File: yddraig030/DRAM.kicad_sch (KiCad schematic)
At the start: 6 parts, among them U1001 XC95108PQ100, U1002 74LS157

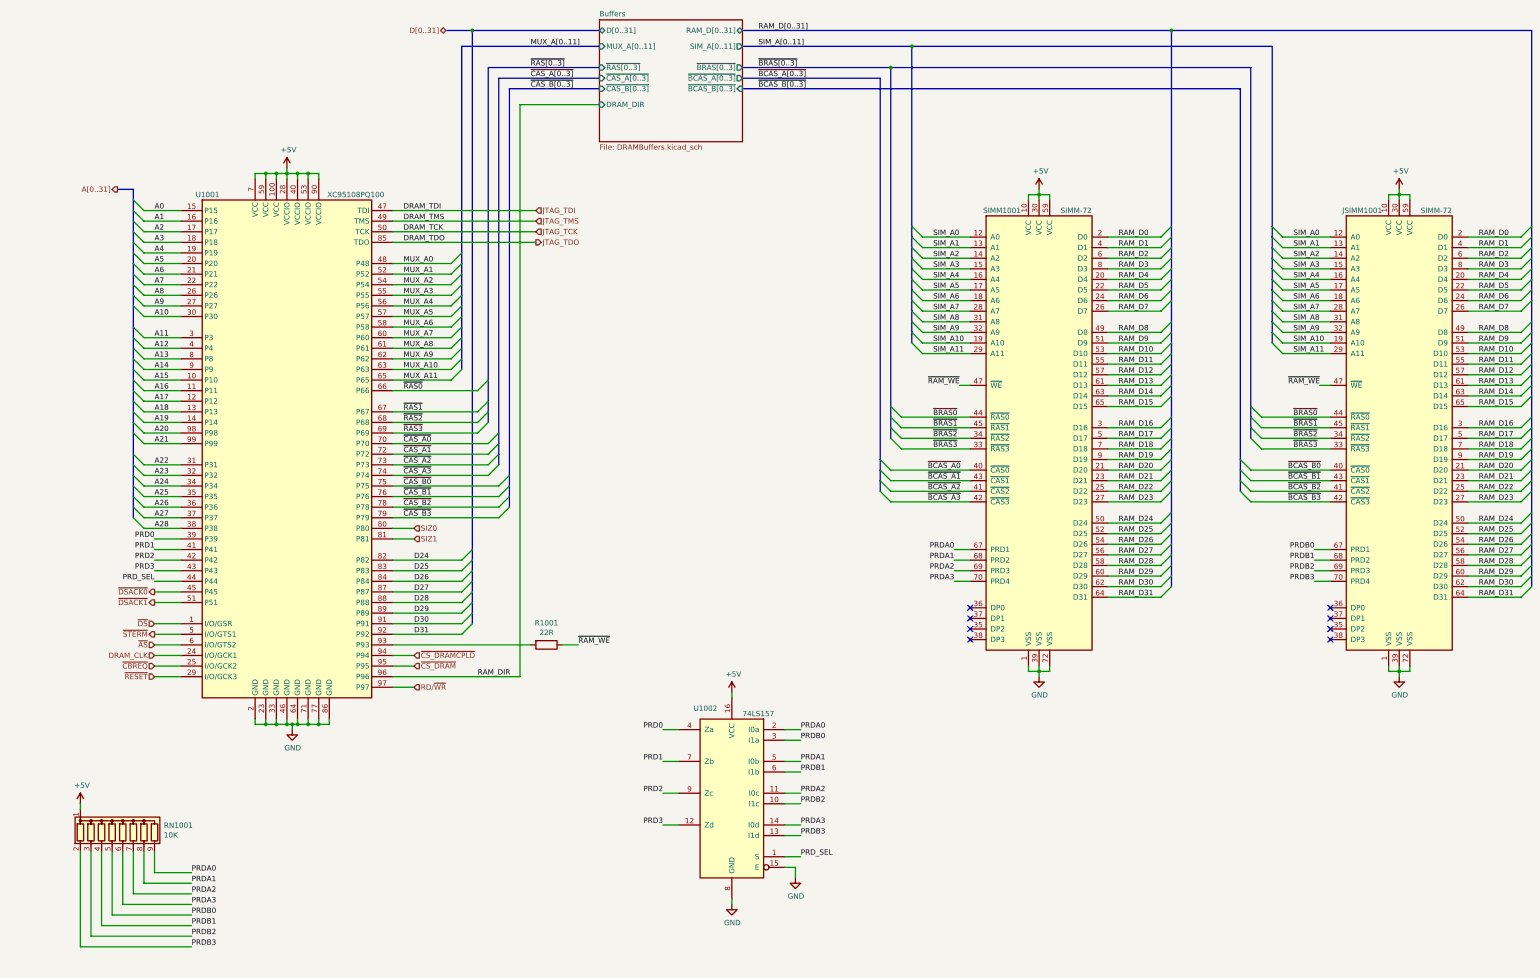
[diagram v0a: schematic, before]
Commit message: More changes to the 030 board
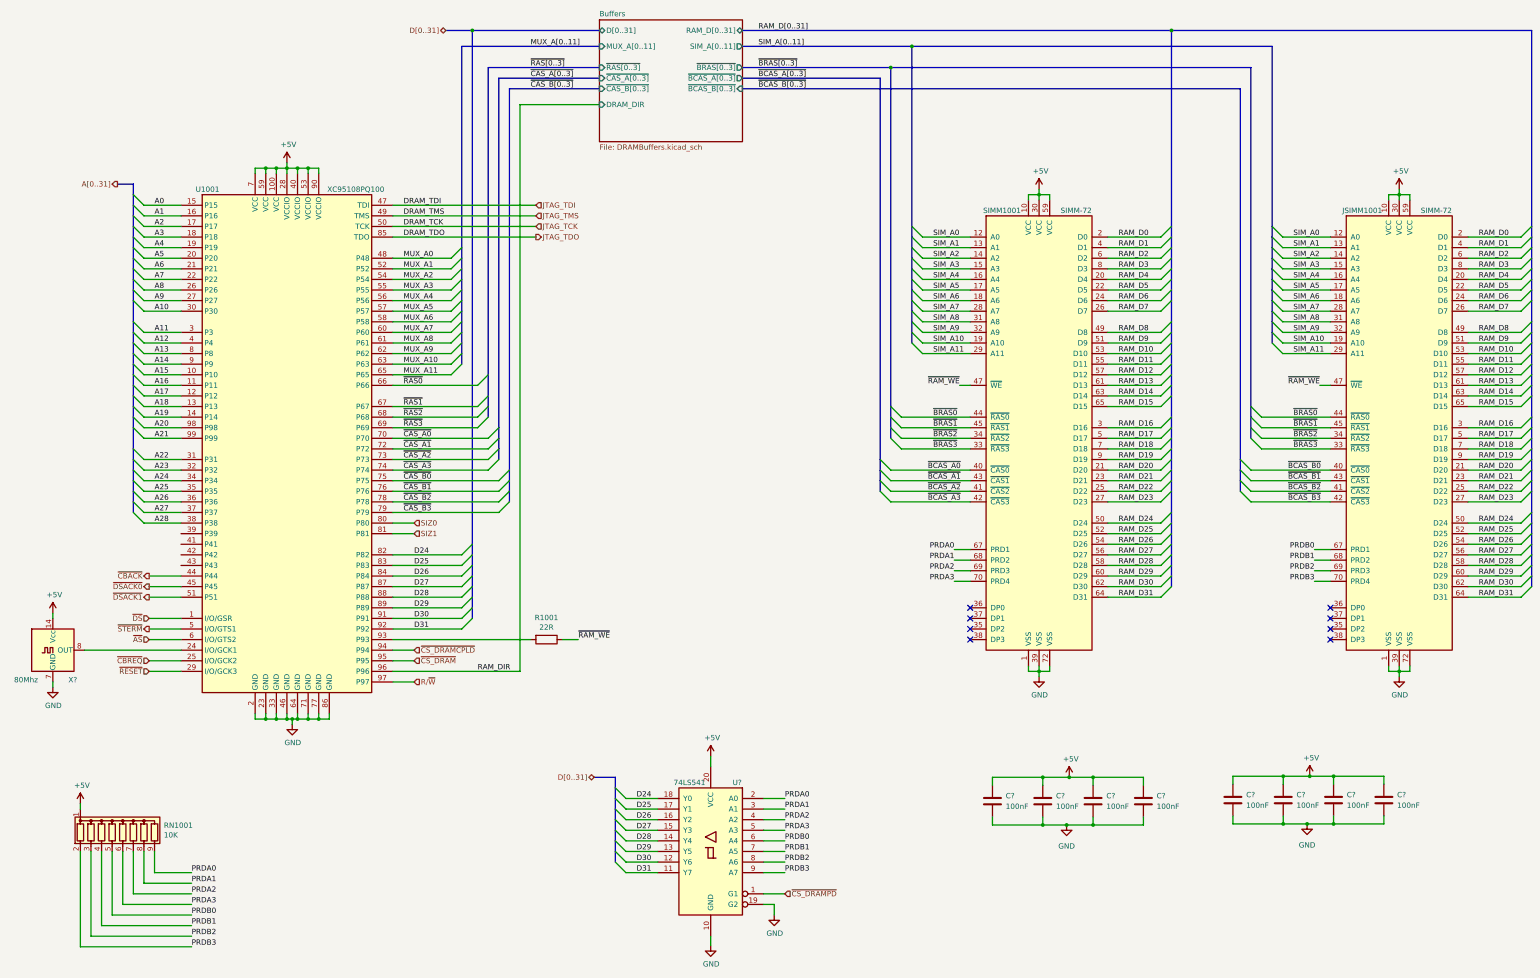
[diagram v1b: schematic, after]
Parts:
- removed U1002: 74LS157, Package_DIP:DIP-16_W7.62mm_Socket, symbol 74xx:74LS157
- added C? (x8): 100nF, symbol Device:C
- added U?: 74LS541, Package_DIP:DIP-20_W7.62mm_Socket, symbol 74xx:74LS541
- added X?: 80Mhz, Oscillator:Oscillator_DIP-14, symbol Oscillator:ACO-xxxMHz
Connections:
- net +5V: now also C?.1, C?.1, C?.1, C?.1, C?.1, C?.1, C?.1, C?.1, U?.20 (VCC), X?.14 (Vcc)
- net D24: now also U?.18 (Y0)
- net D25: now also U?.17 (Y1)
- net D26: now also U?.16 (Y2)
- net D27: now also U?.15 (Y3)
- net D28: now also U?.14 (Y4)
- net D29: now also U?.13 (Y5)
- net D30: now also U?.12 (Y6)
- net D31: now also U?.11 (Y7)
- net GND: now also C?.2, C?.2, C?.2, C?.2, C?.2, C?.2, C?.2, C?.2, U?.10 (GND), U?.19 (G2), X?.7 (GND)
- net PRDA0: now also U?.2 (A0)
- net PRDA1: now also U?.3 (A1)
- net PRDA2: now also U?.4 (A2)
- net PRDA3: now also U?.5 (A3)
- net PRDB0: now also U?.6 (A4)
- net PRDB1: now also U?.7 (A5)
- net PRDB2: now also U?.8 (A6)
- net PRDB3: now also U?.9 (A7)
- net DRAM_CLK: no longer names the net of U1001.24 (I/O/GCK1)
- net DRAM_CLK: now also X?.8 (OUT)
- net PRD0: no longer names the net of U1001.39 (P39)
- net PRD1: no longer names the net of U1001.41 (P41)
- net PRD2: no longer names the net of U1001.42 (P42)
- net PRD3: no longer names the net of U1001.43 (P43)
- net PRD_SEL renamed ~{CBACK}
- net RD/~{WR} renamed R/~{W}
- new net ~{CS_DRAMPD}: U?.1 (G1)
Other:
- moved on the sheet: R1001, U1001

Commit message: ddraig030 schematic done
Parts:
- gave numbers to parts that had none: 10
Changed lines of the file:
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@@
   (symbol (lib_id "power:GND") (at 92.71 213.36 0) (unit 1)
     (in_bom yes) (on_board yes)
-    (property "Reference" "#PWR01003" (id 0) (at 92.71 219.71 0)
+    (property "Reference" "#PWR01005" (id 0) (at 92.71 219.71 0)
       (effects (font (size 1.27 1.27)) hide)
     )
@@
   (symbol (lib_id "power:+5V") (at 91.44 78.74 0) (unit 1)
     (in_bom yes) (on_board yes)
-    (property "Reference" "#PWR01002" (id 0) (at 91.44 82.55 0)
+    (property "Reference" "#PWR01004" (id 0) (at 91.44 82.55 0)
       (effects (font (size 1.27 1.27)) hide)
     )
@@
   (symbol (lib_id "power:+5V") (at 41.91 232.41 0) (unit 1)
     (in_bom yes) (on_board yes)
-    (property "Reference" "#PWR01001" (id 0) (at 41.91 236.22 0)
+    (property "Reference" "#PWR01003" (id 0) (at 41.91 236.22 0)
       (effects (font (size 1.27 1.27)) hide)
     )
@@
   (symbol (lib_id "power:+5V") (at 271.78 85.09 0) (unit 1)
     (in_bom yes) (on_board yes)
-    (property "Reference" "#PWR01007" (id 0) (at 271.78 88.9 0)
+    (property "Reference" "#PWR01009" (id 0) (at 271.78 88.9 0)
       (effects (font (size 1.27 1.27)) hide)
     )
@@
   (symbol (lib_id "power:GND") (at 193.04 266.446 0) (unit 1)
     (in_bom yes) (on_board yes)
-    (property "Reference" "#PWR01005" (id 0) (at 193.04 272.796 0)
+    (property "Reference" "#PWR01007" (id 0) (at 193.04 272.796 0)
       (effects (font (size 1.27 1.27)) hide)
     )
@@
   (symbol (lib_id "power:GND") (at 208.28 259.08 0) (unit 1)
     (in_bom yes) (on_board yes)
-    (property "Reference" "#PWR01006" (id 0) (at 208.28 265.43 0)
+    (property "Reference" "#PWR01008" (id 0) (at 208.28 265.43 0)
       (effects (font (size 1.27 1.27)) hide)
     )
@@
   (symbol (lib_id "power:+5V") (at 193.04 220.98 0) (unit 1)
     (in_bom yes) (on_board yes)
-    (property "Reference" "#PWR01004" (id 0) (at 193.04 224.79 0)
+    (property "Reference" "#PWR01006" (id 0) (at 193.04 224.79 0)
       (effects (font (size 1.27 1.27)) hide)
     )
@@
   (symbol (lib_id "power:GND") (at 271.78 201.93 0) (unit 1)
     (in_bom yes) (on_board yes)
-    (property "Reference" "#PWR01008" (id 0) (at 271.78 208.28 0)
+    (property "Reference" "#PWR01010" (id 0) (at 271.78 208.28 0)
       (effects (font (size 1.27 1.27)) hide)
     )
@@
   (symbol (lib_id "power:+5V") (at 358.14 85.09 0) (unit 1)
     (in_bom yes) (on_board yes)
-    (property "Reference" "#PWR01009" (id 0) (at 358.14 88.9 0)
+    (property "Reference" "#PWR01015" (id 0) (at 358.14 88.9 0)
       (effects (font (size 1.27 1.27)) hide)
     )
@@
   (symbol (lib_id "power:GND") (at 358.14 201.93 0) (unit 1)
     (in_bom yes) (on_board yes)
-    (property "Reference" "#PWR01010" (id 0) (at 358.14 208.28 0)
+    (property "Reference" "#PWR01016" (id 0) (at 358.14 208.28 0)
       (effects (font (size 1.27 1.27)) hide)
     )
@@
   (symbol (lib_id "Device:C") (at 284.734 231.775 0) (unit 1)
     (in_bom yes) (on_board yes) (fields_autoplaced)
-    (property "Reference" "C?" (id 0) (at 287.909 230.5049 0)
+    (property "Reference" "C1003" (id 0) (at 287.909 230.5049 0)
       (effects (font (size 1.27 1.27)) (justify left))
     )
@@
   (symbol (lib_id "power:+5V") (at 35.306 186.69 0) (unit 1)
     (in_bom yes) (on_board yes)
-    (property "Reference" "#PWR?" (id 0) (at 35.306 190.5 0)
+    (property "Reference" "#PWR01001" (id 0) (at 35.306 190.5 0)
       (effects (font (size 1.27 1.27)) hide)
     )
@@
   (symbol (lib_id "Device:C") (at 330.327 231.521 0) (unit 1)
     (in_bom yes) (on_board yes) (fields_autoplaced)
-    (property "Reference" "C?" (id 0) (at 333.502 230.2509 0)
+    (property "Reference" "C1006" (id 0) (at 333.502 230.2509 0)
       (effects (font (size 1.27 1.27)) (justify left))
     )
@@
   (symbol (lib_id "power:+5V") (at 279.019 226.06 0) (unit 1)
     (in_bom yes) (on_board yes)
-    (property "Reference" "#PWR?" (id 0) (at 279.019 229.87 0)
+    (property "Reference" "#PWR01012" (id 0) (at 279.019 229.87 0)
       (effects (font (size 1.27 1.27)) hide)
     )
@@
   (symbol (lib_id "power:GND") (at 336.042 237.236 0) (unit 1)
     (in_bom yes) (on_board yes) (fields_autoplaced)
-    (property "Reference" "#PWR?" (id 0) (at 336.042 243.586 0)
+    (property "Reference" "#PWR01013" (id 0) (at 336.042 243.586 0)
       (effects (font (size 1.27 1.27)) hide)
     )
@@
   (symbol (lib_id "74xx:74LS541") (at 193.04 243.84 0) (mirror y) (unit 1)
     (in_bom yes) (on_board yes)
-    (property "Reference" "U?" (id 0) (at 199.39 227.33 0))
+    (property "Reference" "U1002" (id 0) (at 199.39 227.33 0))
     (property "Value" "74LS541" (id 1) (at 187.96 227.33 0))
     (property "Footprint" "Package_DIP:DIP-20_W7.62mm_Socket" (id 2) (at 193.04 243.84 0)
@@
   (symbol (lib_id "Device:C") (at 296.799 231.775 0) (unit 1)
     (in_bom yes) (on_board yes) (fields_autoplaced)
-    (property "Reference" "C?" (id 0) (at 299.974 230.5049 0)
+    (property "Reference" "C1004" (id 0) (at 299.974 230.5049 0)
       (effects (font (size 1.27 1.27)) (justify left))
     )
@@
   (symbol (lib_id "Device:C") (at 318.262 231.521 0) (unit 1)
     (in_bom yes) (on_board yes) (fields_autoplaced)
-    (property "Reference" "C?" (id 0) (at 321.437 230.2509 0)
+    (property "Reference" "C1005" (id 0) (at 321.437 230.2509 0)
       (effects (font (size 1.27 1.27)) (justify left))
     )
@@
   (symbol (lib_id "power:GND") (at 35.306 204.47 0) (unit 1)
     (in_bom yes) (on_board yes)
-    (property "Reference" "#PWR?" (id 0) (at 35.306 210.82 0)
+    (property "Reference" "#PWR01002" (id 0) (at 35.306 210.82 0)
       (effects (font (size 1.27 1.27)) hide)
     )
@@
   (symbol (lib_id "Device:C") (at 260.604 231.775 0) (unit 1)
     (in_bom yes) (on_board yes) (fields_autoplaced)
-    (property "Reference" "C?" (id 0) (at 263.779 230.5049 0)
+    (property "Reference" "C1001" (id 0) (at 263.779 230.5049 0)
       (effects (font (size 1.27 1.27)) (justify left))
     )
@@
   (symbol (lib_id "Device:C") (at 342.392 231.521 0) (unit 1)
     (in_bom yes) (on_board yes) (fields_autoplaced)
-    (property "Reference" "C?" (id 0) (at 345.567 230.2509 0)
+    (property "Reference" "C1007" (id 0) (at 345.567 230.2509 0)
       (effects (font (size 1.27 1.27)) (justify left))
     )
@@
   (symbol (lib_id "Device:C") (at 354.457 231.521 0) (unit 1)
     (in_bom yes) (on_board yes) (fields_autoplaced)
-    (property "Reference" "C?" (id 0) (at 357.632 230.2509 0)
+    (property "Reference" "C1008" (id 0) (at 357.632 230.2509 0)
       (effects (font (size 1.27 1.27)) (justify left))
     )
@@
   (symbol (lib_id "Oscillator:ACO-xxxMHz") (at 35.306 195.58 0) (unit 1)
     (in_bom yes) (on_board yes)
-    (property "Reference" "X?" (id 0) (at 41.148 202.692 0)
+    (property "Reference" "X1001" (id 0) (at 41.148 202.692 0)
       (effects (font (size 1.27 1.27)) (justify right))
     )
@@
   (symbol (lib_id "power:+5V") (at 336.677 225.806 0) (unit 1)
     (in_bom yes) (on_board yes)
-    (property "Reference" "#PWR?" (id 0) (at 336.677 229.616 0)
+    (property "Reference" "#PWR01014" (id 0) (at 336.677 229.616 0)
       (effects (font (size 1.27 1.27)) hide)
     )
@@
   (symbol (lib_id "Device:C") (at 272.669 231.775 0) (unit 1)
     (in_bom yes) (on_board yes) (fields_autoplaced)
-    (property "Reference" "C?" (id 0) (at 275.844 230.5049 0)
+    (property "Reference" "C1002" (id 0) (at 275.844 230.5049 0)
       (effects (font (size 1.27 1.27)) (justify left))
     )
@@
   (symbol (lib_id "power:GND") (at 278.384 237.49 0) (unit 1)
     (in_bom yes) (on_board yes) (fields_autoplaced)
-    (property "Reference" "#PWR?" (id 0) (at 278.384 243.84 0)
-      (effects (font (size 1.27 1.27)) hide)
-    )
+    (property "Reference" "#PWR01011" (id 0) (at 278.384 243.84 0)
+      (effects (font (size 1.27 1.27)) hide)
+    )

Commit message: Small changes to 030 design
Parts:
- C1001, C1002, C1003, C1004, C1005, C1006, C1007, C1008: footprint (none) -> Capacitor_THT:C_Disc_D3.8mm_W2.6mm_P2.50mm
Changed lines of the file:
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@@
       (effects (font (size 1.27 1.27)) (justify left))
     )
-    (property "Footprint" "" (id 2) (at 285.6992 235.585 0)
+    (property "Footprint" "Capacitor_THT:C_Disc_D3.8mm_W2.6mm_P2.50mm" (id 2) (at 285.6992 235.585 0)
       (effects (font (size 1.27 1.27)) hide)
     )
@@
       (effects (font (size 1.27 1.27)) (justify left))
     )
-    (property "Footprint" "" (id 2) (at 331.2922 235.331 0)
+    (property "Footprint" "Capacitor_THT:C_Disc_D3.8mm_W2.6mm_P2.50mm" (id 2) (at 331.2922 235.331 0)
       (effects (font (size 1.27 1.27)) hide)
     )
@@
       (effects (font (size 1.27 1.27)) (justify left))
     )
-    (property "Footprint" "" (id 2) (at 297.7642 235.585 0)
+    (property "Footprint" "Capacitor_THT:C_Disc_D3.8mm_W2.6mm_P2.50mm" (id 2) (at 297.7642 235.585 0)
       (effects (font (size 1.27 1.27)) hide)
     )
@@
       (effects (font (size 1.27 1.27)) (justify left))
     )
-    (property "Footprint" "" (id 2) (at 319.2272 235.331 0)
+    (property "Footprint" "Capacitor_THT:C_Disc_D3.8mm_W2.6mm_P2.50mm" (id 2) (at 319.2272 235.331 0)
       (effects (font (size 1.27 1.27)) hide)
     )
@@
       (effects (font (size 1.27 1.27)) (justify left))
     )
-    (property "Footprint" "" (id 2) (at 261.5692 235.585 0)
+    (property "Footprint" "Capacitor_THT:C_Disc_D3.8mm_W2.6mm_P2.50mm" (id 2) (at 261.5692 235.585 0)
       (effects (font (size 1.27 1.27)) hide)
     )
@@
       (effects (font (size 1.27 1.27)) (justify left))
     )
-    (property "Footprint" "" (id 2) (at 343.3572 235.331 0)
+    (property "Footprint" "Capacitor_THT:C_Disc_D3.8mm_W2.6mm_P2.50mm" (id 2) (at 343.3572 235.331 0)
       (effects (font (size 1.27 1.27)) hide)
     )
@@
       (effects (font (size 1.27 1.27)) (justify left))
     )
-    (property "Footprint" "" (id 2) (at 355.4222 235.331 0)
+    (property "Footprint" "Capacitor_THT:C_Disc_D3.8mm_W2.6mm_P2.50mm" (id 2) (at 355.4222 235.331 0)
       (effects (font (size 1.27 1.27)) hide)
     )
@@
       (effects (font (size 1.27 1.27)) (justify left))
     )
-    (property "Footprint" "" (id 2) (at 273.6342 235.585 0)
-      (effects (font (size 1.27 1.27)) hide)
-    )
+    (property "Footprint" "Capacitor_THT:C_Disc_D3.8mm_W2.6mm_P2.50mm" (id 2) (at 273.6342 235.585 0)
+      (effects (font (size 1.27 1.27)) hide)
+    )

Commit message: yddraig030: Fixed ERC check errors
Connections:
- no-connect marks 8 -> 12
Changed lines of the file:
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@@
   (no_connect (at 255.27 185.42))
   (no_connect (at 255.27 187.96))
+  (no_connect (at 66.04 175.26))
+  (no_connect (at 66.04 172.72))
+  (no_connect (at 66.04 167.64))
+  (no_connect (at 66.04 170.18))
   (bus_entry (at 133.35 119.38) (size -2.54 2.54)
     (stroke (width 0) (type default) (color 0 0 0 0))
@@
     (stroke (width 0) (type default) (color 0 0 0 0))
   )
+  (wire (pts (xy 243.84 96.52) (xy 255.27 96.52))
+    (stroke (width 0) (type default) (color 0 0 0 0))
+  )
   (bus (pts (xy 135.89 170.18) (xy 135.89 172.72))
     (stroke (width 0) (type default) (color 0 0 0 0))
@@
     (stroke (width 0) (type default) (color 0 0 0 0))
   )
-  (wire (pts (xy 243.84 96.52) (xy 255.27 96.52))
-    (stroke (width 0) (type default) (color 0 0 0 0))
-  )
   (bus (pts (xy 303.53 142.24) (xy 303.53 144.78))
     (stroke (width 0) (type default) (color 0 0 0 0))
@@
     (effects (font (size 1.27 1.27)) (justify left bottom))
   )
-  (label "DRAM_TDI" (at 119.38 88.9 0)
-    (effects (font (size 1.27 1.27)) (justify left bottom))
-  )
   (label "RAM_D22" (at 290.83 157.48 0)
     (effects (font (size 1.27 1.27)) (justify left bottom))
@@
     (effects (font (size 1.27 1.27)) (justify left bottom))
   )
-  (label "DRAM_TCK" (at 119.38 93.98 0)
-    (effects (font (size 1.27 1.27)) (justify left bottom))
-  )
   (label "RAM_D7" (at 290.83 114.3 0)
     (effects (font (size 1.27 1.27)) (justify left bottom))
@@
     (effects (font (size 1.27 1.27)) (justify left bottom))
   )
-  (label "DRAM_TMS" (at 119.38 91.44 0)
-    (effects (font (size 1.27 1.27)) (justify left bottom))
-  )
   (label "RAM_D13" (at 377.19 132.08 0)
     (effects (font (size 1.27 1.27)) (justify left bottom))
@@
     (effects (font (size 1.27 1.27)) (justify left bottom))
   )
-  (label "DRAM_TDO" (at 119.38 96.52 0)
-    (effects (font (size 1.27 1.27)) (justify left bottom))
-  )
   (label "RAM_D18" (at 377.19 147.32 0)
     (effects (font (size 1.27 1.27)) (justify left bottom))
@@
       (effects (font (size 1.27 1.27)) (justify left))
     )
-    (pin "SIM_A[0..11]" output (at 200.66 50.8 0)
-      (effects (font (size 1.27 1.27)) (justify right))
-    )
     (pin "RAM_D[0..31]" bidirectional (at 200.66 46.99 0)
       (effects (font (size 1.27 1.27)) (justify right))
     )
-    (pin "MUX_A[0..11]" input (at 166.37 50.8 180)
-      (effects (font (size 1.27 1.27)) (justify left))
-    )
     (pin "~{RAS[0..3]}" input (at 166.37 55.88 180)
       (effects (font (size 1.27 1.27)) (justify left))
@@
       (effects (font (size 1.27 1.27)) (justify left))
     )
+    (pin "MUX_A[0..11]" input (at 166.37 50.8 180)
+      (effects (font (size 1.27 1.27)) (justify left))
+    )
+    (pin "SIM_A[0..11]" output (at 200.66 50.8 0)
+      (effects (font (size 1.27 1.27)) (justify right))
+    )
   )
